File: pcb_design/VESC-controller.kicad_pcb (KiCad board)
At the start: 2 copper layers, 160 x 92.5 mm, 183 parts, among them J1 GATE_DRIVER_CONN_U, J2 GATE_DRIVER_CONN_V, J3 GATE_DRIVER_CONN_W, J4 micro USB, J5 ACCEL, J6 REGEN, J7 12V, P1 HALL/Encoder, P101 CANBUS, P3 PWR_COMM, Q1 BSC340N08, U1 STM32F40X_LQFP64, U10 LM2903-SO8, U11 LM3488, U12 OPA2376AID, U13 LM1117IMP-v.v, U16 OPA2376AID, U17 LM2903-SO8, U2 ISO1050, U3 OPA2376AID, U4 LM2903-SO8, U5 7400-TSSOP, U6 SN74ALVC08PWR, U7 SN74ALVC08PWR, U8 SN74AUP1G74, U9 LM22676QTJ-5.0, X2 ABM3B - 8MHz

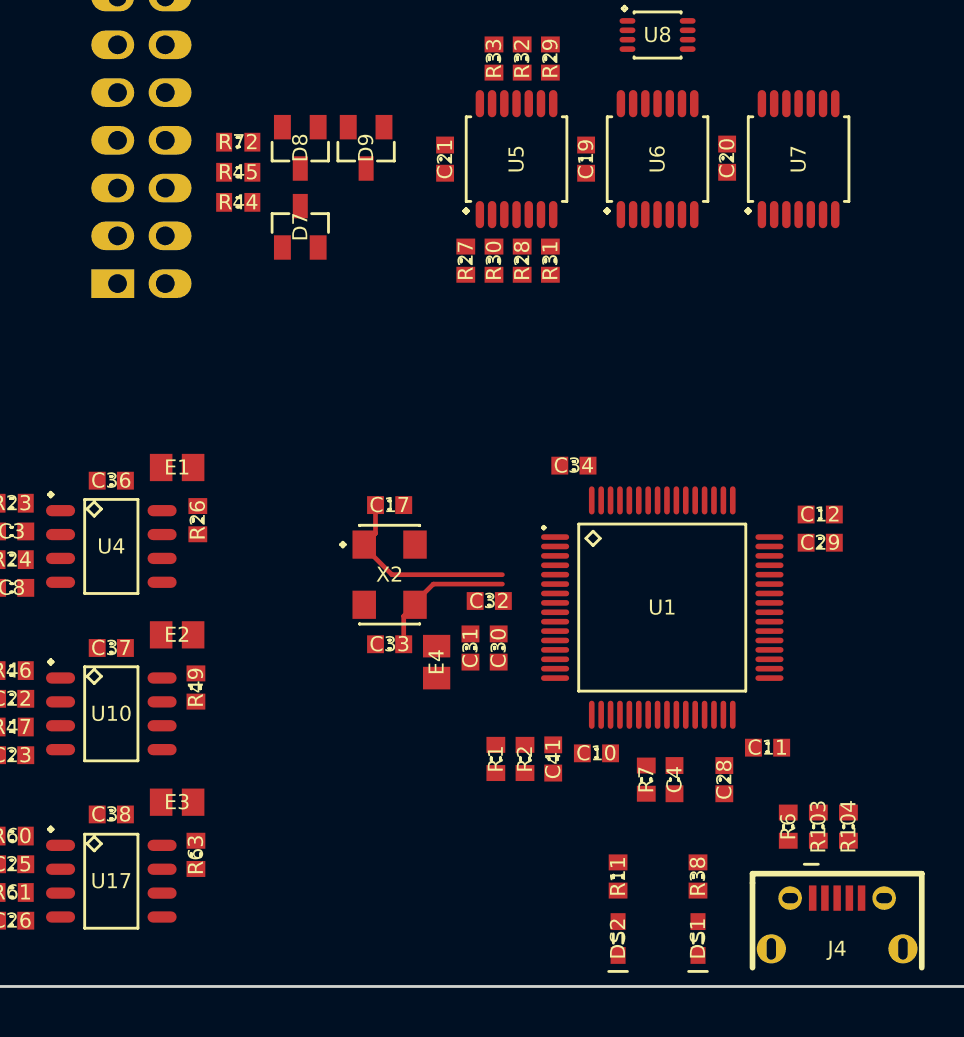
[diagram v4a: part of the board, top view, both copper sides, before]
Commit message: Added lp filters, fuses, tvs and power symbols
Signed-off-by: Marcos Chaparro <mchaparro@paltatech.com>
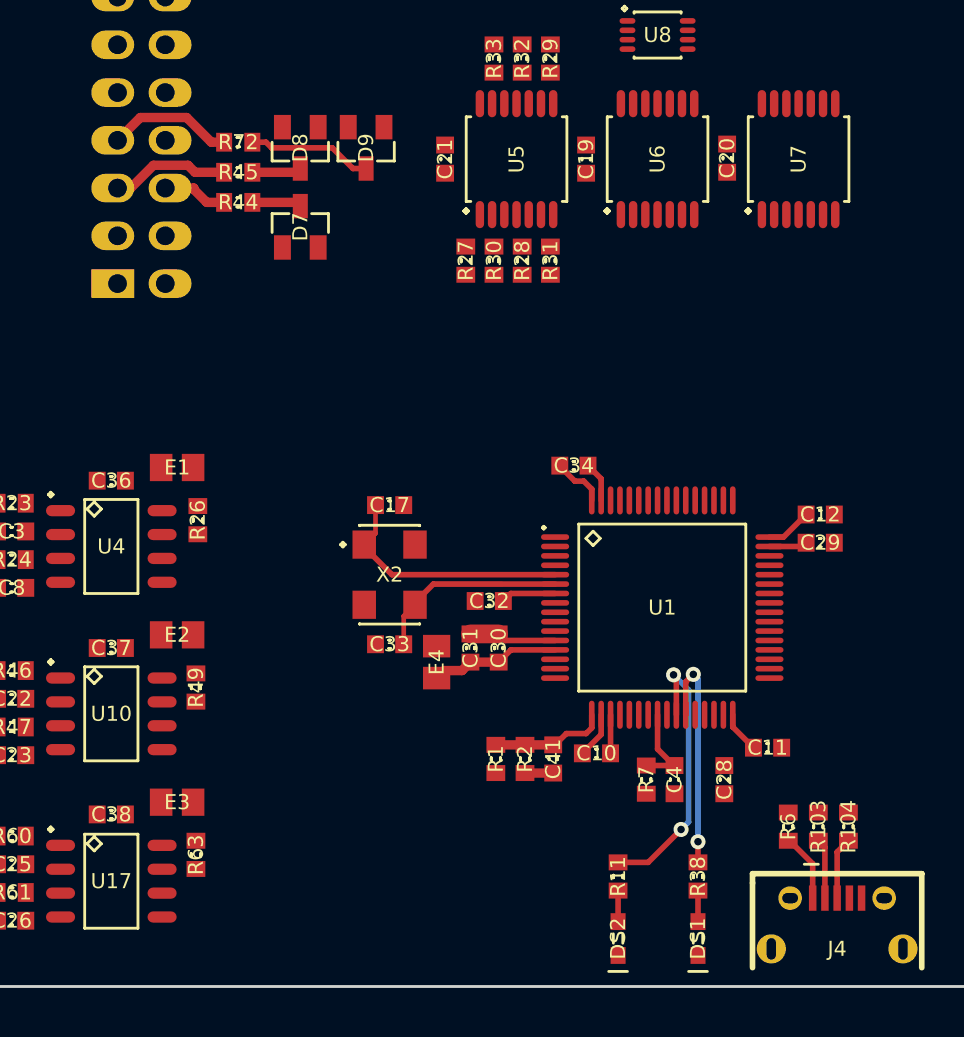
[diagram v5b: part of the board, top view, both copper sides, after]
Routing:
- net /STM32F4/LED_GREEN: track 0.00 -> 15.0 mm, vias 0 -> 2
- net /STM32F4/LED_RED: track 0.00 -> 12.4 mm, vias 0 -> 2
- net GND: track 0.00 -> 10.7 mm
- net VCC: track 3.02 -> 12.6 mm
- net Net-(C17-Pad2): track 10.4 -> 19.1 mm
- net Net-(C30-Pad1): track 0.00 -> 6.92 mm
- net /conditioning V/Power_good: track 0.00 -> 6.72 mm
- net Net-(D9-Pad3): track 0.00 -> 6.63 mm
- net Net-(C33-Pad2): track 7.53 -> 14.0 mm
- net /conditioning V/PWM_GB: track 0.00 -> 6.33 mm
- net /STM32F4/ADC_TEMP: track 0.00 -> 6.17 mm
- net /Filters/TEMP_IN: track 0.00 -> 4.59 mm
- net Net-(J4-Pad1): track 0.00 -> 3.63 mm
- net /conditioning V/PWM_GT: track 0.00 -> 3.49 mm
- net Net-(J4-Pad3): track 0.00 -> 3.30 mm
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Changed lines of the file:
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@@
   (general
     (links 435)
-    (no_connects 422)
+    (no_connects 423)
     (area -80.275001 -45.275001 80.390501 47.845)
     (thickness 1.6)
     (drawings 2)
-    (tracks 41)
+    (tracks 129)
     (zones 0)
     (modules 183)
@@
   )
   (setup
-    (last_trace_width 1)
+    (last_trace_width 0.5)
     (user_trace_width 0.3)
     (user_trace_width 0.5)
@@
       (effects (font (size 1.5 1.5) (thickness 0.3)))
     )
-    (fp_text value HALL/Encoder (at -12.29924 -6.9 360) (layer F.SilkS)
+    (fp_text value HALL/Encoder (at -12.29924 -6.9) (layer F.SilkS)
       (effects (font (size 1.5 1.5) (thickness 0.3)))
     )
@@
     (effects (font (size 1.5 1.5) (thickness 0.3)))
   )
+  (segment (start 13.4 33.65) (end 14.9 33.65) (width 0.5) (layer F.Cu) (net 6))
+  (segment (start 12 26.25) (end 10.5 26.25) (width 1) (layer F.Cu) (net 6))
+  (segment (start 15 26.6) (end 12.35 26.6) (width 0.3) (layer F.Cu) (net 6))
+  (segment (start 12.35 26.6) (end 12 26.25) (width 0.3) (layer F.Cu) (net 6))
+  (segment (start 17.45 19.15) (end 17.45 18) (width 0.3) (layer F.Cu) (net 6))
+  (segment (start 17.45 18) (end 16.75 17.3) (width 0.3) (layer F.Cu) (net 6))
+  (segment (start 17.45 30.55) (end 17.45 31.6) (width 0.3) (layer F.Cu) (net 6))
+  (segment (start 17.45 31.6) (end 16.45 32.6) (width 0.3) (layer F.Cu) (net 6))
+  (segment (start 16.525001 18.125001) (end 16.050001 18.125001) (width 0.3) (layer F.Cu) (net 7))
+  (segment (start 16.050001 18.125001) (end 15.25 17.325) (width 0.3) (layer F.Cu) (net 7))
+  (segment (start 15.25 17.325) (end 15.25 17.3) (width 0.3) (layer F.Cu) (net 7))
+  (segment (start 16.95 18.55) (end 16.525001 18.125001) (width 0.3) (layer F.Cu) (net 7))
+  (segment (start 16.95 19.15) (end 16.95 18.55) (width 0.3) (layer F.Cu) (net 7))
+  (segment (start 26.4 21.1) (end 27.15 21.1) (width 0.3) (layer F.Cu) (net 7))
+  (segment (start 27.15 21.1) (end 28.35 19.9) (width 0.3) (layer F.Cu) (net 7))
+  (segment (start 24.45 30.55) (end 24.45 31.2) (width 0.3) (layer F.Cu) (net 7))
+  (segment (start 24.45 31.2) (end 25.55 32.3) (width 0.3) (layer F.Cu) (net 7))
+  (segment (start 17.95 30.55) (end 17.95 32.6) (width 0.3) (layer F.Cu) (net 7))
   (segment (start 53.862 20) (end 53.862 22.948) (width 1) (layer F.Cu) (net 7))
   (segment (start 53.862 22.948) (end 53.81 23) (width 1) (layer F.Cu) (net 7))
+  (segment (start -1.1 1.7) (end 1.25 1.7) (width 0.5) (layer F.Cu) (net 10))
+  (segment (start 1.25 1.7) (end 1.45 1.5) (width 0.5) (layer F.Cu) (net 10))
+  (segment (start -2.6 0.1) (end -3.28096 0.1) (width 0.5) (layer F.Cu) (net 15))
+  (segment (start -3.28096 0.1) (end -4.59297 -1.21201) (width 0.5) (layer F.Cu) (net 15))
+  (segment (start -4.59297 -1.21201) (end -7.05799 -1.21201) (width 0.5) (layer F.Cu) (net 15))
+  (segment (start -7.05799 -1.21201) (end -8.27 0) (width 0.5) (layer F.Cu) (net 15))
+  (segment (start -1.1 3.3) (end 1.25 3.3) (width 0.5) (layer F.Cu) (net 16))
+  (segment (start 1.25 3.3) (end 1.45 3.5) (width 0.5) (layer F.Cu) (net 16))
   (segment (start 50 34.25) (end 50 33.25) (width 0.5) (layer F.Cu) (net 19))
   (via (at 50 33.25) (size 0.8) (drill 0.4) (layers F.Cu B.Cu) (net 19))
@@
   (segment (start 53.81 32.6) (end 53.81 35.06) (width 1) (layer F.Cu) (net 22))
   (segment (start 53.81 35.06) (end 53.85 35.1) (width 1) (layer F.Cu) (net 22))
+  (segment (start -4.21 2.54) (end -4.21 2.615) (width 0.5) (layer F.Cu) (net 32))
+  (segment (start -4.21 2.615) (end -3.525 3.3) (width 0.5) (layer F.Cu) (net 32))
+  (segment (start -3.525 3.3) (end -2.6 3.3) (width 0.5) (layer F.Cu) (net 32))
+  (segment (start -5.73 2.54) (end -4.21 2.54) (width 0.5) (layer F.Cu) (net 32))
+  (segment (start -2.6 1.7) (end -4.15 1.7) (width 0.5) (layer F.Cu) (net 34))
+  (segment (start -4.15 1.7) (end -4.52201 1.32799) (width 0.5) (layer F.Cu) (net 34))
+  (segment (start -8.27 2.54) (end -7.57104 2.54) (width 0.5) (layer F.Cu) (net 34))
+  (segment (start -7.57104 2.54) (end -6.35903 1.32799) (width 0.5) (layer F.Cu) (net 34))
+  (segment (start -6.35903 1.32799) (end -4.52201 1.32799) (width 0.5) (layer F.Cu) (net 34))
+  (segment (start 20.45 30.55) (end 20.45 32.375) (width 0.3) (layer F.Cu) (net 40))
+  (segment (start 20.45 32.375) (end 21.325 33.25) (width 0.3) (layer F.Cu) (net 40))
+  (segment (start 21.325 33.25) (end 21.35 33.25) (width 0.3) (layer F.Cu) (net 40))
+  (segment (start 21.35 33.25) (end 19.85 33.25) (width 0.3) (layer F.Cu) (net 40))
+  (segment (start 22.6 39.9) (end 22.6 41.55084) (width 0.3) (layer F.Cu) (net 57))
+  (segment (start 18.35 39.9) (end 18.35 41.55084) (width 0.3) (layer F.Cu) (net 58))
+  (segment (start 15 23.1) (end 6.325 23.1) (width 0.3) (layer F.Cu) (net 107))
+  (segment (start 6.325 23.1) (end 4.85 21.625) (width 0.3) (layer F.Cu) (net 107))
+  (segment (start 4.85 21.625) (end 4.85 21.5) (width 0.3) (layer F.Cu) (net 107))
   (segment (start 5.45 19.4) (end 5.45 20.9) (width 0.25) (layer F.Cu) (net 107))
   (segment (start 5.45 20.9) (end 4.85 21.5) (width 0.25) (layer F.Cu) (net 107))
   (segment (start 12.2 23.1) (end 6.325 23.1) (width 0.25) (layer F.Cu) (net 107))
-  (segment (start 6.325 23.1) (end 4.85 21.625) (width 0.25) (layer F.Cu) (net 107))
-  (segment (start 4.85 21.625) (end 4.85 21.5) (width 0.25) (layer F.Cu) (net 107))
+  (segment (start 15 23.6) (end 8.525 23.6) (width 0.3) (layer F.Cu) (net 108))
+  (segment (start 8.525 23.6) (end 7.55 24.575) (width 0.3) (layer F.Cu) (net 108))
+  (segment (start 7.55 24.575) (end 7.55 24.7) (width 0.3) (layer F.Cu) (net 108))
   (segment (start 6.95 26.8) (end 6.95 25.3) (width 0.25) (layer F.Cu) (net 108))
   (segment (start 6.95 25.3) (end 7.55 24.7) (width 0.25) (layer F.Cu) (net 108))
   (segment (start 12.2 23.6) (end 8.525 23.6) (width 0.25) (layer F.Cu) (net 108))
-  (segment (start 8.525 23.6) (end 7.55 24.575) (width 0.25) (layer F.Cu) (net 108))
-  (segment (start 7.55 24.575) (end 7.55 24.7) (width 0.25) (layer F.Cu) (net 108))
+  (segment (start 15 24.1) (end 12.65 24.1) (width 0.3) (layer F.Cu) (net 110))
+  (segment (start 12.65 24.1) (end 12.25 24.5) (width 0.3) (layer F.Cu) (net 110))
+  (segment (start 13.4 32.15) (end 11.85 32.15) (width 0.5) (layer F.Cu) (net 111))
+  (segment (start 14.9 32.15) (end 15 32.15) (width 0.3) (layer F.Cu) (net 111))
+  (segment (start 15 32.15) (end 15.6 31.55) (width 0.3) (layer F.Cu) (net 111))
+  (segment (start 15.6 31.55) (end 16.65 31.55) (width 0.3) (layer F.Cu) (net 111))
+  (segment (start 16.65 31.55) (end 16.95 31.25) (width 0.3) (layer F.Cu) (net 111))
+  (segment (start 16.95 31.25) (end 16.95 30.55) (width 0.3) (layer F.Cu) (net 111))
+  (segment (start 13.4 32.15) (end 14.9 32.15) (width 0.5) (layer F.Cu) (net 111))
+  (segment (start 21.7 36.65) (end 19.95 38.4) (width 0.3) (layer F.Cu) (net 112))
+  (segment (start 19.95 38.4) (end 18.35 38.4) (width 0.3) (layer F.Cu) (net 112))
+  (segment (start 22.09999 36.25001) (end 21.7 36.65) (width 0.3) (layer B.Cu) (net 112))
+  (via (at 21.7 36.65) (size 0.8) (drill 0.4) (layers F.Cu B.Cu) (net 112))
+  (segment (start 22.09999 29.225785) (end 22.09999 36.25001) (width 0.3) (layer B.Cu) (net 112))
+  (segment (start 21.300014 28.425809) (end 22.09999 29.225785) (width 0.3) (layer B.Cu) (net 112))
+  (segment (start 21.45 30.55) (end 21.45 28.575795) (width 0.3) (layer F.Cu) (net 112))
+  (segment (start 21.45 28.575795) (end 21.300014 28.425809) (width 0.3) (layer F.Cu) (net 112))
+  (via (at 21.300014 28.425809) (size 0.8) (drill 0.4) (layers F.Cu B.Cu) (net 112))
+  (segment (start 22.35 28.4) (end 21.95 28.8) (width 0.3) (layer F.Cu) (net 113))
+  (segment (start 21.95 28.8) (end 21.95 30.55) (width 0.3) (layer F.Cu) (net 113))
+  (segment (start 22.6 37.3) (end 22.6 28.65) (width 0.3) (layer B.Cu) (net 113))
+  (segment (start 22.6 28.65) (end 22.35 28.4) (width 0.3) (layer B.Cu) (net 113))
+  (via (at 22.35 28.4) (size 0.8) (drill 0.4) (layers F.Cu B.Cu) (net 113))
+  (segment (start 22.6 38.4) (end 22.6 37.3) (width 0.3) (layer F.Cu) (net 113))
+  (via (at 22.6 37.3) (size 0.8) (drill 0.4) (layers F.Cu B.Cu) (net 113))
+  (segment (start 26.4 21.6) (end 28.15 21.6) (width 0.3) (layer F.Cu) (net 120))
+  (segment (start 28.15 21.6) (end 28.35 21.4) (width 0.3) (layer F.Cu) (net 120))
+  (segment (start 28.7 40.3) (end 28.7 38.475) (width 0.3) (layer F.Cu) (net 131))
+  (segment (start 28.7 38.475) (end 27.475 37.25) (width 0.3) (layer F.Cu) (net 131))
+  (segment (start 27.475 37.25) (end 27.4 37.25) (width 0.3) (layer F.Cu) (net 131))
+  (segment (start 29.35 40.3) (end 29.35 37.6) (width 0.3) (layer F.Cu) (net 132))
+  (segment (start 29.35 37.6) (end 29 37.25) (width 0.3) (layer F.Cu) (net 132))
+  (segment (start 30 40.3) (end 30 37.85) (width 0.3) (layer F.Cu) (net 133))
+  (segment (start 30 37.85) (end 30.6 37.25) (width 0.3) (layer F.Cu) (net 133))
+  (segment (start -0.075 0.4) (end 3.15 0.4) (width 0.3) (layer F.Cu) (net 138))
+  (segment (start 3.15 0.4) (end 4.25 1.5) (width 0.3) (layer F.Cu) (net 138))
+  (segment (start 4.25 1.5) (end 4.95 1.5) (width 0.3) (layer F.Cu) (net 138))
+  (segment (start -1.1 0.1) (end -0.375 0.1) (width 0.3) (layer F.Cu) (net 138))
+  (segment (start -0.375 0.1) (end -0.075 0.4) (width 0.3) (layer F.Cu) (net 138))
   (segment (start 50 36.8) (end 51.5 36.8) (width 0.5) (layer F.Cu) (net 140))
   (segment (start 48.5 36.8) (end 50 36.8) (width 0.5) (layer F.Cu) (net 140))
+  (segment (start 10.5 27.75) (end 10.05 28.2) (width 0.5) (layer F.Cu) (net 141))
+  (segment (start 10.05 28.2) (end 9.1 28.2) (width 0.5) (layer F.Cu) (net 141))
+  (segment (start 9.1 28.2) (end 8.7 28.6) (width 0.5) (layer F.Cu) (net 141))
+  (segment (start 12 27.75) (end 10.5 27.75) (width 0.5) (layer F.Cu) (net 141))
+  (segment (start 15 27.1) (end 12.65 27.1) (width 0.3) (layer F.Cu) (net 141))
+  (segment (start 12.65 27.1) (end 12 27.75) (width 0.3) (layer F.Cu) (net 141))
 )
